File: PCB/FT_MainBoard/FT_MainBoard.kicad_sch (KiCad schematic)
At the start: 7 parts

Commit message: update mb shematic
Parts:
- added CON_CTRL: Conn_01x03_Pin, Connector:FanPinHeader_1x03_P2.54mm_Vertical, symbol Connector:Conn_01x03_Pin
- added CON_TARGETS: Conn_01x04_Pin, Connector:FanPinHeader_1x04_P2.54mm_Vertical, symbol Connector:Conn_01x04_Pin
- added C_MCU_OSC1, C_MCU_OSC2: 22pF, symbol Device:C
- added C_USB1: 100nF, symbol Device:C
- added C_USB2, C_USB3: 47pF, symbol Device:C
- added J1: USB_B, symbol Connector:USB_B
- added MCU_OSC: 16MHz, Crystal:Crystal_SMD_HC49-SD_HandSoldering, symbol Device:Crystal
- added R_USB_D+, R_USB_D-: 27R, symbol Device:R
- added Y2: Crystal, Crystal:Crystal_SMD_HC49-SD_HandSoldering, symbol Device:Crystal
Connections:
- net +12V: now also CON_TARGETS.1 (Pin_1)
- net GND: now also CON_CTRL.1 (Pin_1), CON_TARGETS.2 (Pin_2), C_MCU_OSC1.2, C_MCU_OSC2.2, C_USB1.1, C_USB2.1, C_USB3.1, J1.4 (GND), J1.5 (Shield)
- net LEFT: now also RL.2, CON_TARGETS.3 (Pin_3); no longer RL.1
- net RIGHT: now also RR.2, CON_TARGETS.4 (Pin_4); no longer RR.1
- net at OPTL.1: now also RL.1; no longer RL.2
- net at OPTR.1: now also RR.1; no longer RR.2
- net at MCU.7 (XTAL1/PB6): now also C_MCU_OSC1.1, MCU_OSC.2
- net at MCU.8 (XTAL2/PB7): now also C_MCU_OSC2.1, MCU_OSC.1
- net at UART-USB.11 (USBDP): now also R_USB_D-.1
- net at UART-USB.12 (USBDM): now also R_USB_D+.1
- net at UART-USB.13 (3V3OUT): now also UART-USB.14 (~{RESET}), UART-USB.3 (VCCIO), C_USB1.2
- net RESET renamed STOP/RES
- net STOP/RES: now also CON_CTRL.3 (Pin_3)
- net START/STOP renamed START
- net START: now also CON_CTRL.2 (Pin_2)
- new net USB_D+: C_USB3.2, J1.3 (D+), R_USB_D+.2
- new net USB_D-: C_USB2.2, J1.2 (D-), R_USB_D-.2
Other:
- moved on the sheet: LREG, MCU, OPTL, OPTR, RL, RR, UART-USB

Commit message: main board corruption fix
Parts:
- removed Y2: Crystal, Crystal:Crystal_SMD_HC49-SD_HandSoldering, symbol Device:Crystal
- added CON_DISPLAY1: Conn_01x08_Pin, Connector_PinSocket_2.54mm:PinSocket_1x08_P2.54mm_Vertical, symbol Connector:Conn_01x08_Pin
- added CON_VIN1: Conn_01x03_Pin, Connector:FanPinHeader_1x03_P2.54mm_Vertical, symbol Connector:Conn_01x03_Pin
- added C_LREG1, C_MCU1, C_VIN2: 100nF, Capacitor_SMD:C_0603_1608Metric_Pad1.08x0.95mm_HandSolder, symbol Device:C
- added C_VIN1: 100uF, Capacitor_SMD:C_1206_3216Metric_Pad1.33x1.80mm_HandSolder, symbol Device:C
- added C_VIN3: 1nF, Capacitor_SMD:C_0603_1608Metric_Pad1.08x0.95mm_HandSolder, symbol Device:C
- added LED_PWR1: RED, LED_SMD:LED_0603_1608Metric_Pad1.05x0.95mm_HandSolder, symbol Device:LED
- added LED_RX1: YELLOW, LED_SMD:LED_0603_1608Metric_Pad1.05x0.95mm_HandSolder, symbol Device:LED
- added LED_TX1: GREEN, LED_SMD:LED_0603_1608Metric_Pad1.05x0.95mm_HandSolder, symbol Device:LED
- added R1, R2, R3: 330R, Resistor_SMD:R_0603_1608Metric_Pad0.98x0.95mm_HandSolder, symbol Device:R
- added R_RES1: 4.7k, Resistor_SMD:R_0603_1608Metric_Pad0.98x0.95mm_HandSolder, symbol Device:R
- C_MCU_OSC1, C_MCU_OSC2, C_USB1, C_USB2, C_USB3: footprint (none) -> Capacitor_SMD:C_0603_1608Metric_Pad1.08x0.95mm_HandSolder
- MCU_OSC1: renamed from MCU_OSC; footprint Crystal:Crystal_SMD_HC49-SD_HandSoldering -> Crystal:Crystal_SMD_3225-4Pin_3.2x2.5mm_HandSoldering
- R_USB1: renamed from R_USB_D-; footprint (none) -> Resistor_SMD:R_0603_1608Metric_Pad0.98x0.95mm_HandSolder
- R_USB2: renamed from R_USB_D+; footprint (none) -> Resistor_SMD:R_0603_1608Metric_Pad0.98x0.95mm_HandSolder
- USB1: renamed from J1; footprint (none) -> Connector_USB:USB_B_Lumberg_2411_02_Horizontal
- renumbered CON_CTRL to CON_CTRL1, CON_TARGETS to CON_TARGETS1, LREG to LREG1, MCU to MCU1, OPTL to OPTL1, OPTR to OPTR1, RL to RL1, RR to RR1, UART-USB to UART-USB1
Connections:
- net +12V: now also CON_VIN1.1 (Pin_1), C_VIN1.1, C_VIN2.1, C_VIN3.1
- net +5V: now also MCU1.18 (AVCC), CON_DISPLAY1.1 (Pin_1), C_LREG1.1, C_MCU1.1, LED_RX1.2 (A), LED_TX1.2 (A), R1.1, R_RES1.2
- net GND: now also CON_DISPLAY1.2 (Pin_2), CON_VIN1.2 (Pin_2), C_LREG1.2, C_MCU1.2, C_VIN1.2, C_VIN2.2, C_VIN3.2, LED_PWR1.1 (K)
- net OPTL>MCU: now also MCU1.32 (PD2); no longer MCU1.30 (PD0)
- net OPTR>MCU: now also MCU1.1 (PD3); no longer MCU1.31 (PD1)
- net at MCU1.12 (PB0): now also CON_DISPLAY1.8 (Pin_8)
- net at MCU1.13 (PB1): now also CON_DISPLAY1.7 (Pin_7)
- net at MCU1.14 (PB2): now also CON_DISPLAY1.6 (Pin_6)
- net at MCU1.15 (PB3): now also CON_DISPLAY1.5 (Pin_5)
- net at MCU1.16 (PB4): now also CON_DISPLAY1.4 (Pin_4)
- net at MCU1.17 (PB5): now also CON_DISPLAY1.3 (Pin_3)
- net at MCU1.29 (~{RESET}/PC6): now also R_RES1.1
- net at UART-USB1.17 (CBUS1): now also R3.2
- net at UART-USB1.18 (CBUS0): now also R2.2
- net TXD: now reaches UART-USB1.20 (TXD)
- net TXD: now also MCU1.31 (PD1)
- net RXD: now reaches UART-USB1.4 (RXD)
- net RXD: now also MCU1.30 (PD0)
- new net: LED_PWR1.2 (A), R1.2
- new net: LED_TX1.1 (K), R2.1
- new net: LED_RX1.1 (K), R3.1
- no-connect marks 7 -> 23
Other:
- moved on the sheet: C_USB1, C_USB2, C_USB3, LREG1, OPTL1, OPTR1, RL1, RR1, R_USB1, R_USB2, UART-USB1, USB1

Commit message: hal, switch
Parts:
- removed CON_VIN1: Conn_01x03_Pin, Connector:FanPinHeader_1x03_P2.54mm_Vertical, symbol Connector:Conn_01x03_Pin
- added CON_VIN: Conn_01x02_Pin, Connector_PinHeader_2.54mm:PinHeader_1x02_P2.54mm_Horizontal, symbol Connector:Conn_01x02_Pin
- CON_CTRL1: footprint Connector:FanPinHeader_1x03_P2.54mm_Vertical -> Connector_PinHeader_2.54mm:PinHeader_1x03_P2.54mm_Horizontal
- CON_TARGETS1: footprint Connector:FanPinHeader_1x04_P2.54mm_Vertical -> Connector_PinHeader_2.54mm:PinHeader_1x04_P2.54mm_Horizontal
- RL1, RR1: value 1K -> 500R
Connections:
- net +12V: now also CON_VIN.1 (Pin_1)
- net GND: now also CON_VIN.2 (Pin_2)
- no-connect marks 23 -> 22

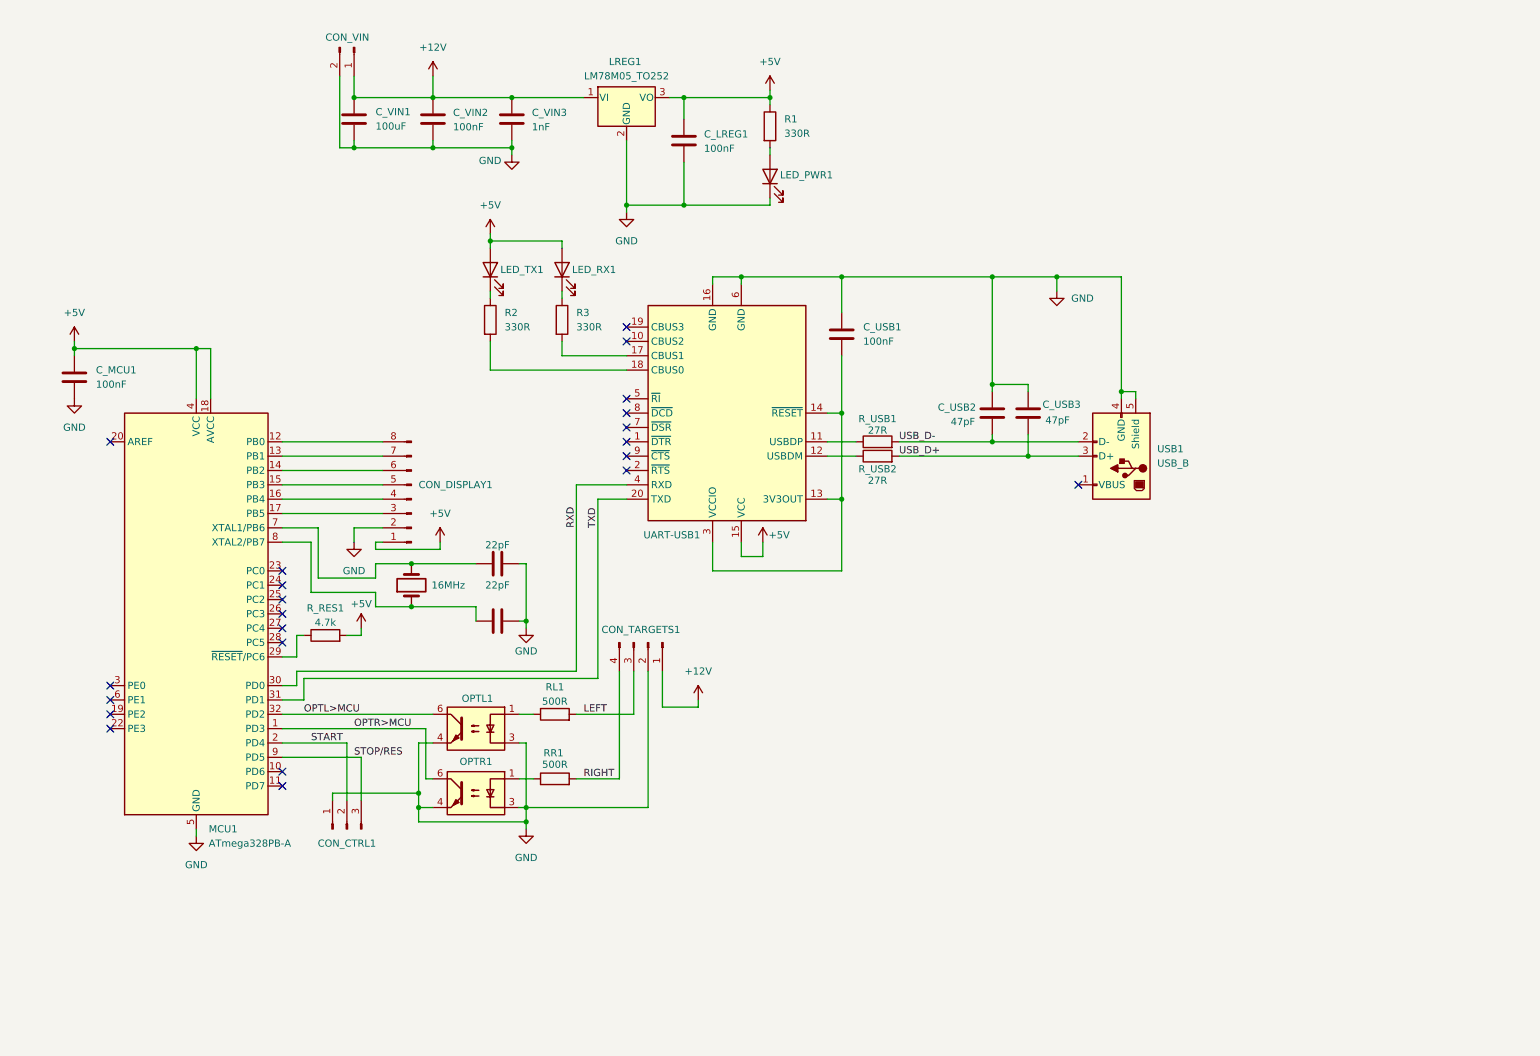
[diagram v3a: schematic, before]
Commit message: create main board PCB
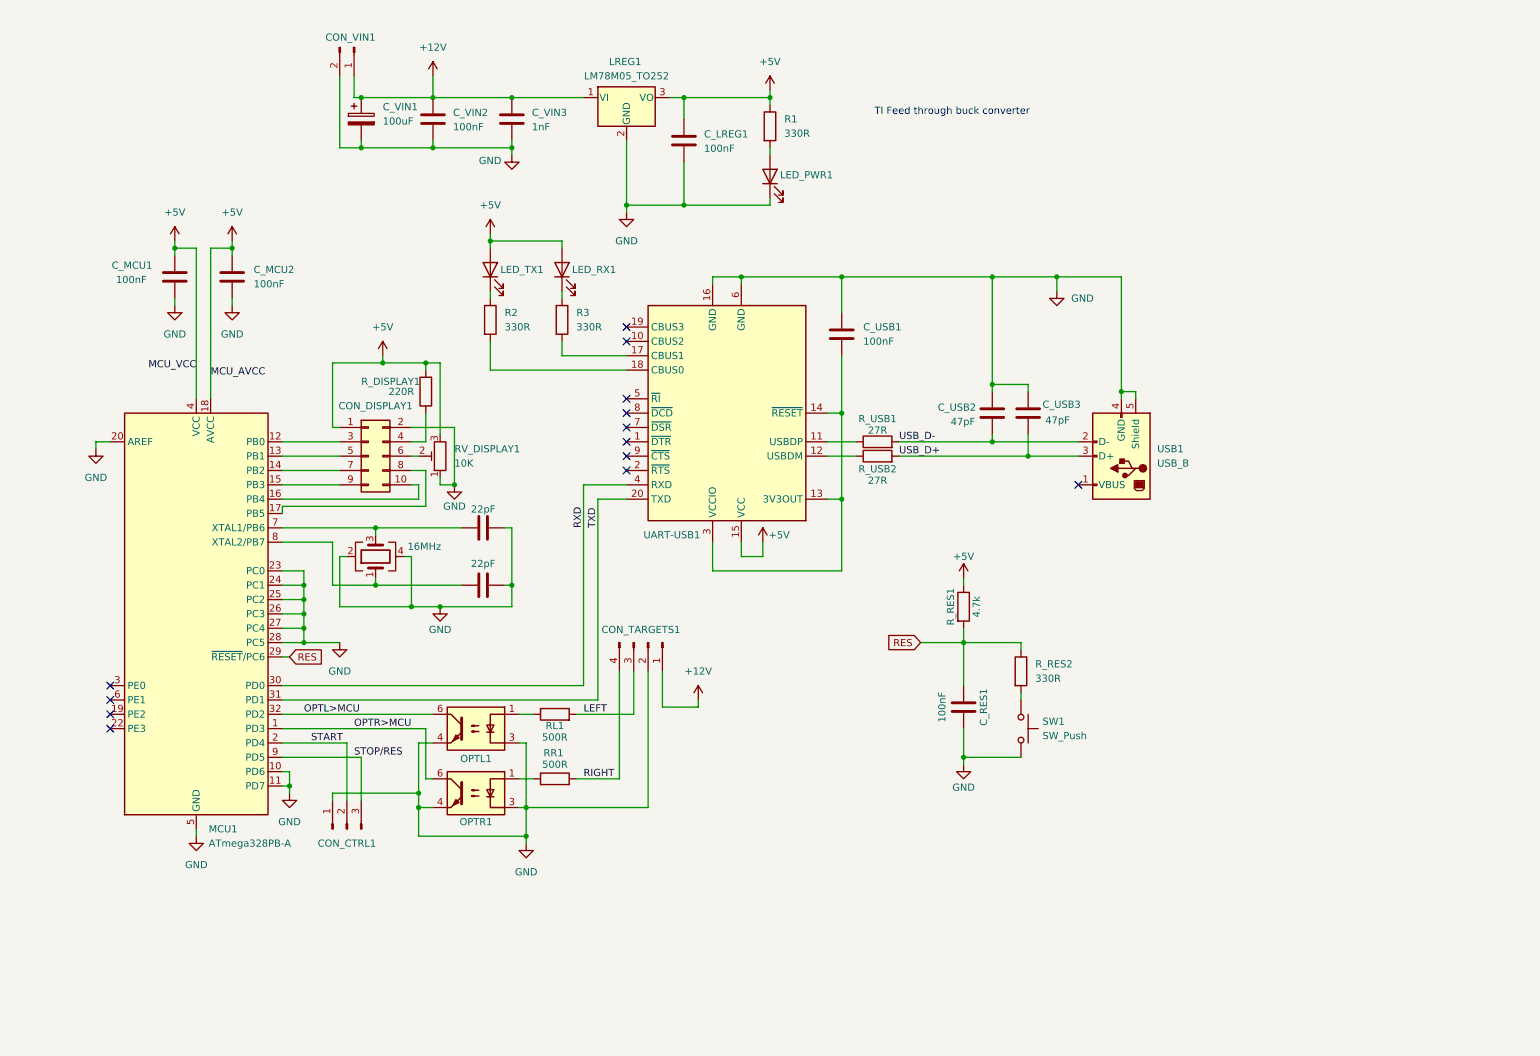
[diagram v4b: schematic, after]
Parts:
- removed CON_DISPLAY1: Conn_01x08_Pin, Connector_PinSocket_2.54mm:PinSocket_1x08_P2.54mm_Vertical, symbol Connector:Conn_01x08_Pin
- removed C_VIN1: 100uF, Capacitor_SMD:C_1206_3216Metric_Pad1.33x1.80mm_HandSolder, symbol Device:C
- removed MCU_OSC1: 16MHz, Crystal:Crystal_SMD_3225-4Pin_3.2x2.5mm_HandSoldering, symbol Device:Crystal
- added CON_DISPLAY1: Conn_02x05_Odd_Even, Connector_PinHeader_2.54mm:PinHeader_2x05_P2.54mm_Horizontal, symbol Connector_Generic:Conn_02x05_Odd_Even
- added C_MCU2, C_RES1: 100nF, Capacitor_SMD:C_0603_1608Metric, symbol Device:C
- added C_VIN1: 100uF, Capacitor_SMD:CP_Elec_5x5.8, symbol Device:C_Polarized
- added OSC_MCU1: 16MHz, Crystal:Crystal_SMD_3225-4Pin_3.2x2.5mm, symbol Device:Crystal_GND24
- added RV_DISPLAY1: 10K, Potentiometer_SMD:Potentiometer_Bourns_TC33X_Vertical, symbol Device:R_Potentiometer_Trim
- added R_DISPLAY1: 220R, Resistor_SMD:R_0603_1608Metric, symbol Device:R
- added R_RES2: 330R, Resistor_SMD:R_0603_1608Metric, symbol Device:R
- added SW1: SW_Push, Button_Switch_SMD:SW_SPST_B3U-1000P, symbol Switch:SW_Push
- C_LREG1, C_MCU1, C_MCU_OSC1, C_MCU_OSC2, C_USB1, C_USB2, C_USB3, C_VIN2, C_VIN3: footprint Capacitor_SMD:C_0603_1608Metric_Pad1.08x0.95mm_HandSolder -> Capacitor_SMD:C_0603_1608Metric
- LED_PWR1, LED_RX1, LED_TX1: footprint LED_SMD:LED_0603_1608Metric_Pad1.05x0.95mm_HandSolder -> LED_SMD:LED_0603_1608Metric
- R1, R2, R3, RL1, RR1, R_RES1, R_USB1, R_USB2: footprint Resistor_SMD:R_0603_1608Metric_Pad0.98x0.95mm_HandSolder -> Resistor_SMD:R_0603_1608Metric
- renumbered CON_VIN to CON_VIN1
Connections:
- net +12V: now also C_VIN1.1
- net +5V: now also R_RES1.1, CON_DISPLAY1.1 (Pin_1), C_MCU2.1, RV_DISPLAY1.3, R_DISPLAY1.2; no longer R_RES1.2
- net GND: now also MCU1.10 (PD6), MCU1.11 (PD7), MCU1.20 (AREF), MCU1.23 (PC0), MCU1.24 (PC1), MCU1.25 (PC2), MCU1.26 (PC3), MCU1.27 (PC4), MCU1.28 (PC5), CON_DISPLAY1.2 (Pin_2), C_MCU2.2, C_RES1.2, C_VIN1.2, OSC_MCU1.2, OSC_MCU1.4, RV_DISPLAY1.1, SW1.2
- net RES: now reaches MCU1.29 (~{RESET}/PC6)
- net RES: now also R_RES1.2, C_RES1.1, R_RES2.1; no longer R_RES1.1
- net at C_MCU_OSC1.1, MCU1.7 (XTAL1/PB6): now also OSC_MCU1.3
- net at C_MCU_OSC2.1, MCU1.8 (XTAL2/PB7): now also OSC_MCU1.1
- net at MCU1.12 (PB0): now also CON_DISPLAY1.3 (Pin_3)
- net at MCU1.13 (PB1): now also CON_DISPLAY1.5 (Pin_5)
- net at MCU1.14 (PB2): now also CON_DISPLAY1.7 (Pin_7)
- net at MCU1.15 (PB3): now also CON_DISPLAY1.9 (Pin_9)
- net at MCU1.16 (PB4): now also CON_DISPLAY1.10 (Pin_10)
- net at MCU1.17 (PB5): now also CON_DISPLAY1.8 (Pin_8)
- new net: CON_DISPLAY1.4 (Pin_4), R_DISPLAY1.1
- new net: CON_DISPLAY1.6 (Pin_6), RV_DISPLAY1.2
- new net: R_RES2.2, SW1.1
- no-connect marks 22 -> 13
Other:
- note added: "TI Feed through buck converter"
- moved on the sheet: C_MCU1

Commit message: update pcbs
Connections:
- net GND: now also MCU1.19 (PE2), MCU1.22 (PE3), MCU1.3 (PE0), MCU1.6 (PE1)
- net DISPLAY_D1: now reaches MCU1.16 (PB4)
- net DISPLAY_D1: now also CON_DISPLAY1.5 (Pin_5); no longer CON_DISPLAY1.10 (Pin_10)
- net DISPLAY_D0: now reaches CON_DISPLAY1.3 (Pin_3)
- net DISPLAY_D0: now also MCU1.17 (PB5); no longer MCU1.12 (PB0)
- net DISPLAY_EN: now reaches MCU1.13 (PB1)
- net DISPLAY_EN: now also CON_DISPLAY1.10 (Pin_10); no longer CON_DISPLAY1.5 (Pin_5)
- net DISPLAY_D2: now reaches CON_DISPLAY1.7 (Pin_7)
- net DISPLAY_D2: now also MCU1.15 (PB3); no longer MCU1.14 (PB2)
- net DISPLAY_RS: now reaches CON_DISPLAY1.8 (Pin_8)
- net DISPLAY_RS: now also MCU1.12 (PB0); no longer MCU1.17 (PB5)
- net DISPLAY_D3: now reaches CON_DISPLAY1.9 (Pin_9)
- net DISPLAY_D3: now also MCU1.14 (PB2); no longer MCU1.15 (PB3)
- no-connect marks 13 -> 9
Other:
- moved on the sheet: CON_DISPLAY1, C_RES1, RV_DISPLAY1, R_DISPLAY1, R_RES1, R_RES2, SW1
